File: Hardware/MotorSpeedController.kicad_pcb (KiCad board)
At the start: 4 copper layers, 25.4 x 25.4 mm, 21 parts, among them J1 Conn_01x08_Female, J2 Conn_01x04_Female, U1 ATmega328P-AU, U2 AS5134, Y1 16MHz

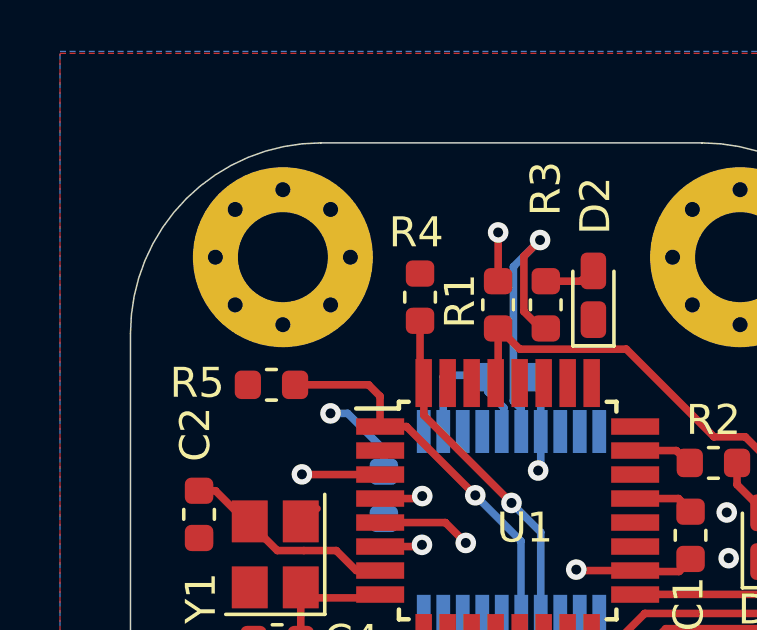
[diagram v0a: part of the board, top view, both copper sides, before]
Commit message: Updated Footprints for better fit
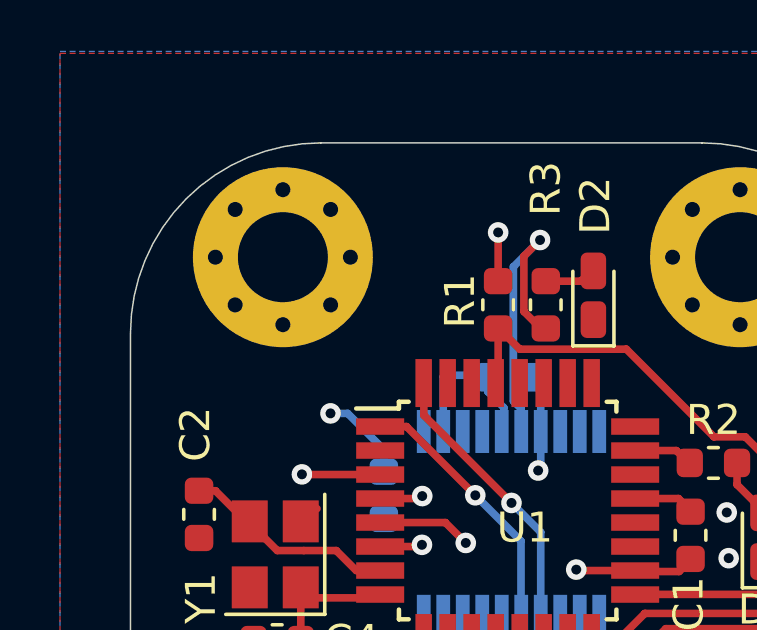
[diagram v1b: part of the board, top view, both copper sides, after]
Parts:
- removed R4, R5: 1k, Resistor_SMD:R_0603_1608Metric
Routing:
- net INT1: track 12.8 -> 8.82 mm
- net INT0: track 11.6 -> 9.55 mm

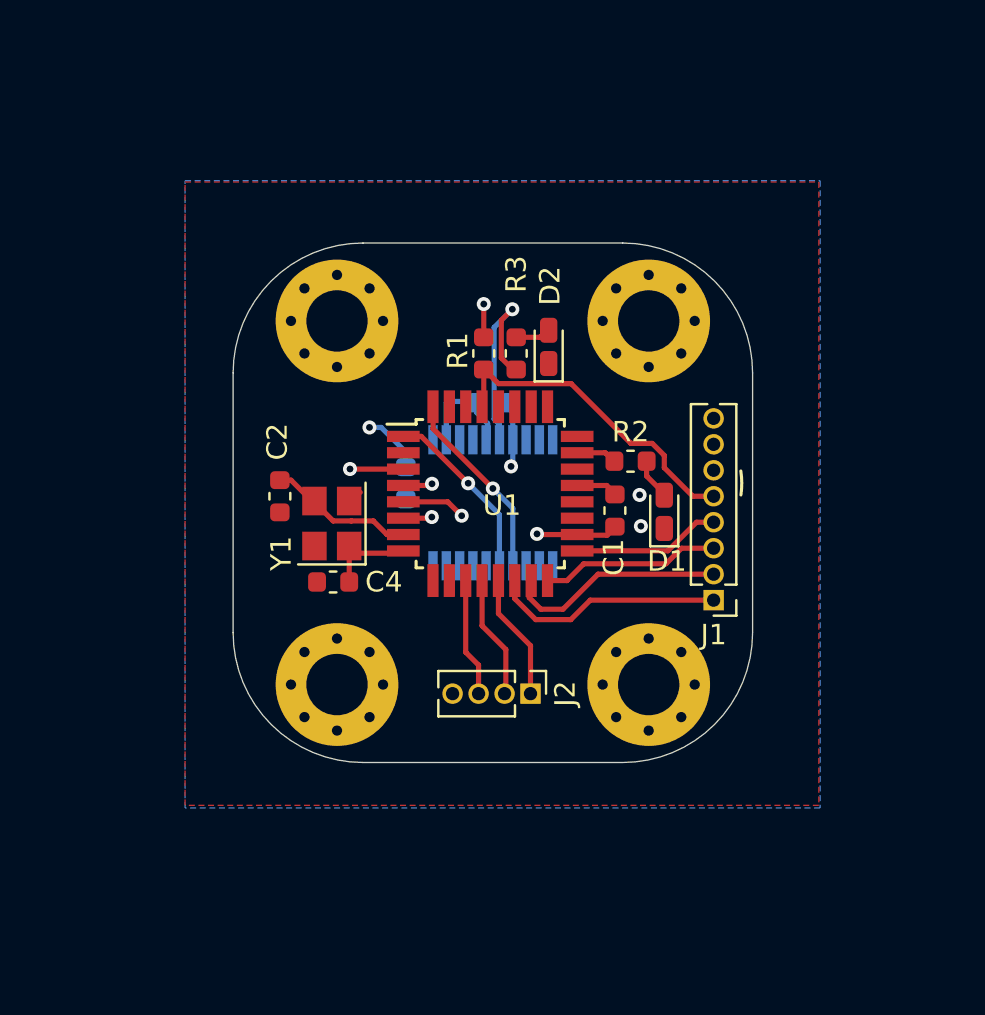
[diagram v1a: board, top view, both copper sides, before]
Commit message: Changed PCB Dimensions. Added +5V regulator. Made headers bigger
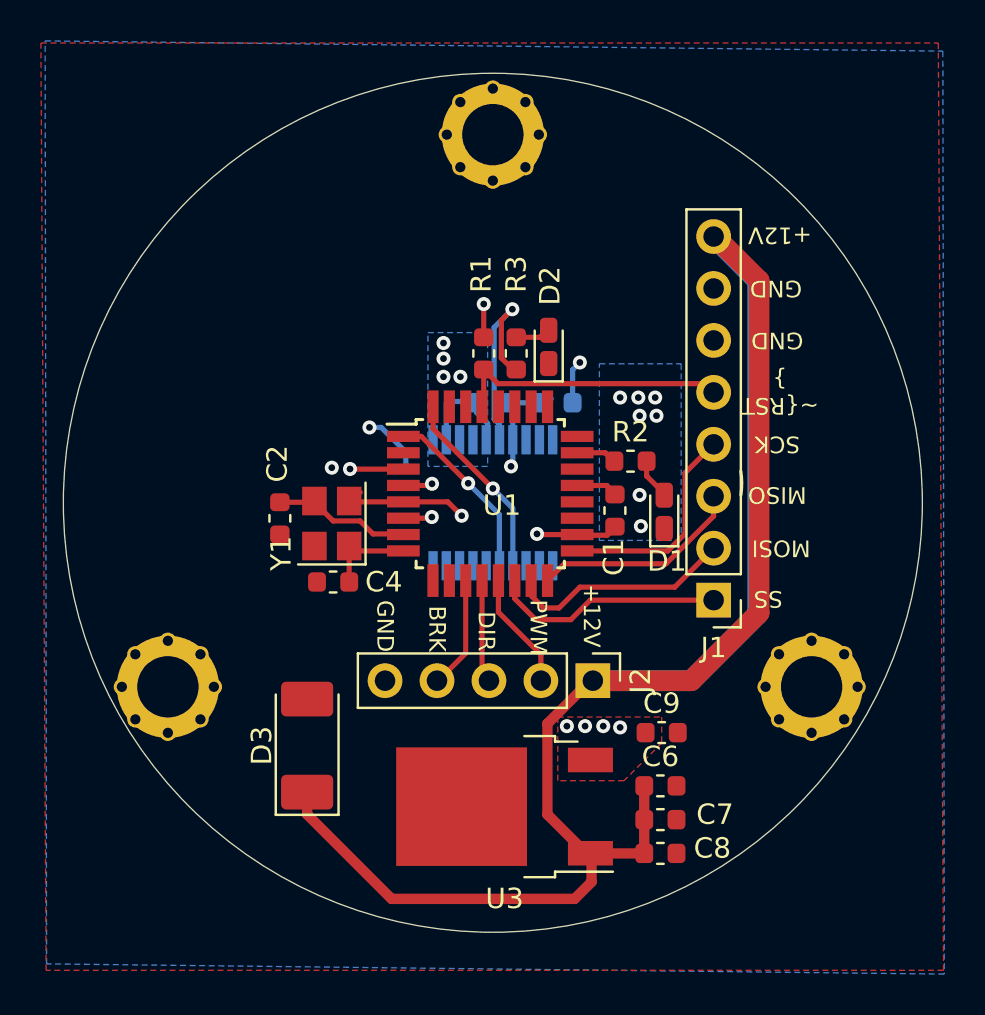
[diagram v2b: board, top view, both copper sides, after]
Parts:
- removed H4: MountingHole_Pad, MountingHole:MountingHole_3mm_Pad_Via
- added C6: 0.1uF, Capacitor_SMD:C_0603_1608Metric, F.Cu at (122.5, 102.7)
- added C7: 0.1uF, Capacitor_SMD:C_0603_1608Metric, F.Cu at (122.5, 104.4)
- added C8: 0.1uF, Capacitor_SMD:C_0603_1608Metric, F.Cu at (122.5, 106.0)
- added C9: 1uF, Capacitor_SMD:C_0603_1608Metric, F.Cu at (122.6, 100.1)
- added D3: D_Small, Diode_SMD:D_2010_5025Metric_Castellated, F.Cu at (105.2, 100.8)
- added U3: MC7805, Package_TO_SOT_SMD:TO-252-2, F.Cu at (114.9, 103.8)
- J1: footprint Connector_PinHeader_1.27mm:PinHeader_1x08_P1.27mm_Vertical -> Connector_PinHeader_2.54mm:PinHeader_1x08_P2.54mm_Vertical
- J2: value Conn_01x04_Female -> Conn_01x05_Female; footprint Connector_PinHeader_1.27mm:PinHeader_1x04_P1.27mm_Vertical -> Connector_PinHeader_2.54mm:PinHeader_1x05_P2.54mm_Vertical
- moved H2 27.9 mm to (114.3, 70.9)
- moved H1 19.7 mm to (98.4, 97.9)
- moved H3 19.6 mm to (129.9, 97.9)
- moved C3 8.35 mm to (117.4, 84.0), turned to 0 degrees
- moved J2 3.11 mm to (119.2, 97.6)
- moved C2 1.08 mm to (103.9, 89.7)
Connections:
- J1 pad 8: +5V -> +12V
- J2 pad 1: PWM -> +12V
- J2 pad 2: DIR -> PWM
- J2 pad 3: BRAKE -> DIR
- J2 pad 4: GND -> BRAKE
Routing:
- net +12V: track 0.00 -> 98.3 mm
- net GND: track 13.2 -> 17.9 mm, vias 4 -> 15
- net SCK: track 7.31 -> 10.5 mm
- net ~RST: track 16.1 -> 13.5 mm
- net +5V: track 14.7 -> 16.8 mm, vias 6 -> 10
- net MISO: track 8.78 -> 10.5 mm
- net DIR: track 6.01 -> 5.12 mm
- net BRAKE: track 6.26 -> 5.45 mm
- net /XTAL2: track 4.12 -> 4.63 mm
- added copper zone on B.Cu, net +5V
- added copper zone on F.Cu, net +5V
- removed copper zone on In2.Cu, net +5V
- removed copper zone on In1.Cu, net GND
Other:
- board size 25.4 x 25.4 mm -> 42 x 42 mm
- copper layers 4 -> 2
- board text added: "+12V"
- board text added: "BRK"
- board text removed: "+5V"
- board text removed: "BRAKE"

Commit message: Added Final CAM files and updated BOM
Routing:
- net GND: track 17.9 -> 20.6 mm, vias 15 -> 13
- net /XTAL1: track 7.19 -> 9.56 mm

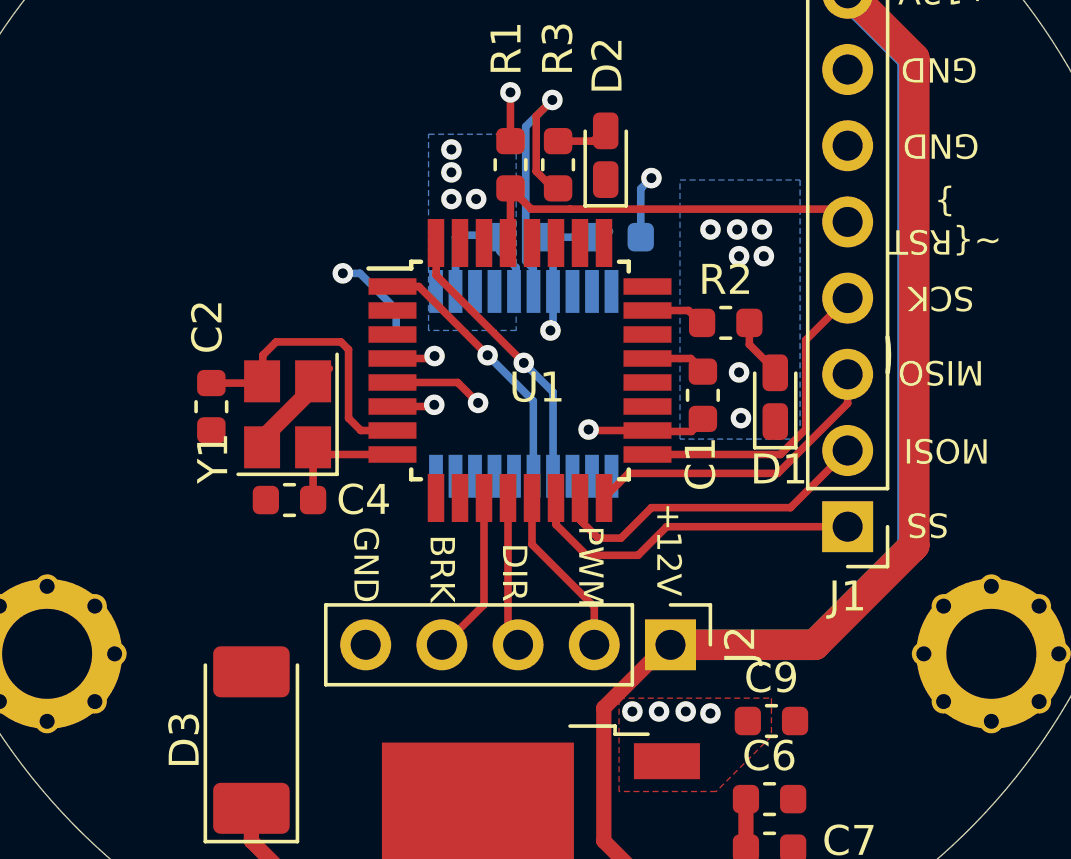
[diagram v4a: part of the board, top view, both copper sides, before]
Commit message: Updated to KiCAD 6
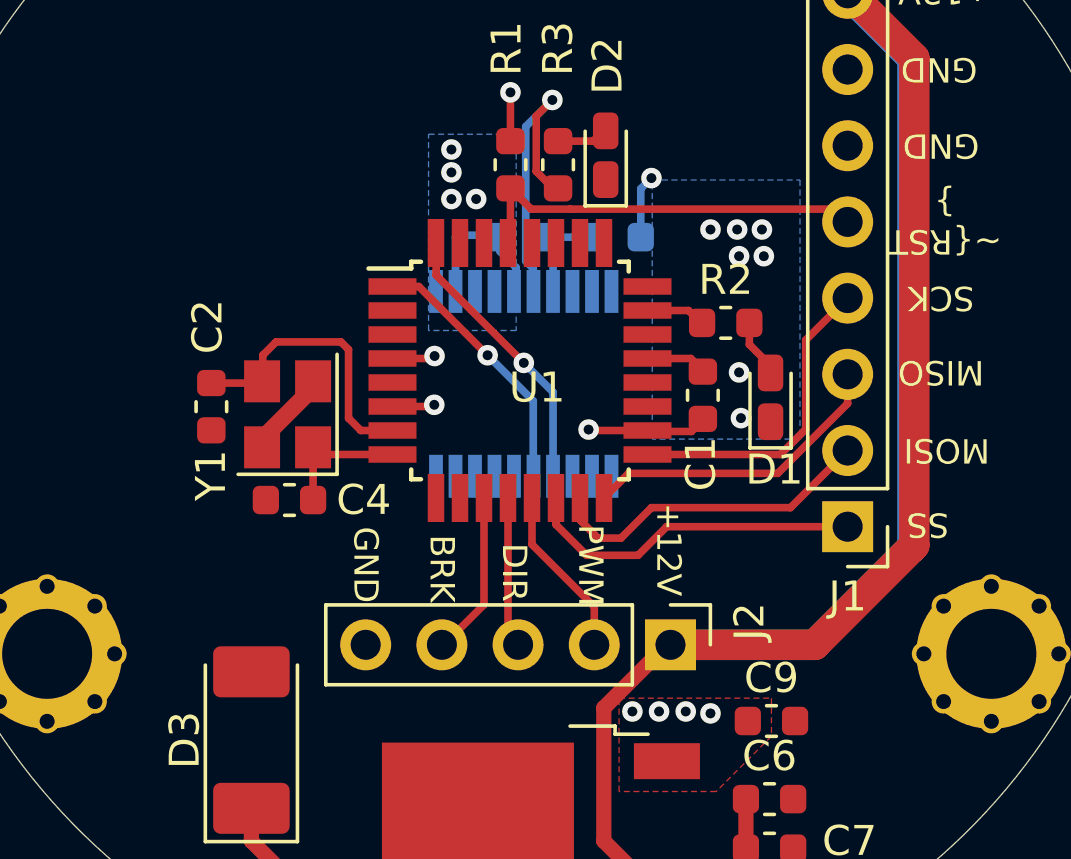
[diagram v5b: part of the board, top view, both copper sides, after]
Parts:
- moved D1 0.16 mm to (122.5, 89.3)
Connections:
- net ~RST renamed ~{RST}
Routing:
- net +5V: track 16.8 -> 12.2 mm, vias 10 -> 8
- net GND: track 20.6 -> 17.2 mm, vias 13 -> 12
- net /XTAL2: track 4.63 -> 3.94 mm
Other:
- net class Default removed
- board text added: "~{RST }"
- board text removed: "~RST"
